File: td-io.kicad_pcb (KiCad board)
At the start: 2 copper layers, 66.5 x 54 mm, 15 parts, among them J1 Conn_02x10_Odd_Even, J2 USB_B, J3 Conn_01x03, J4 Conn_01x02, Q1 AO4818B, U1 Pico, U2 ISL3175EIBZ-T

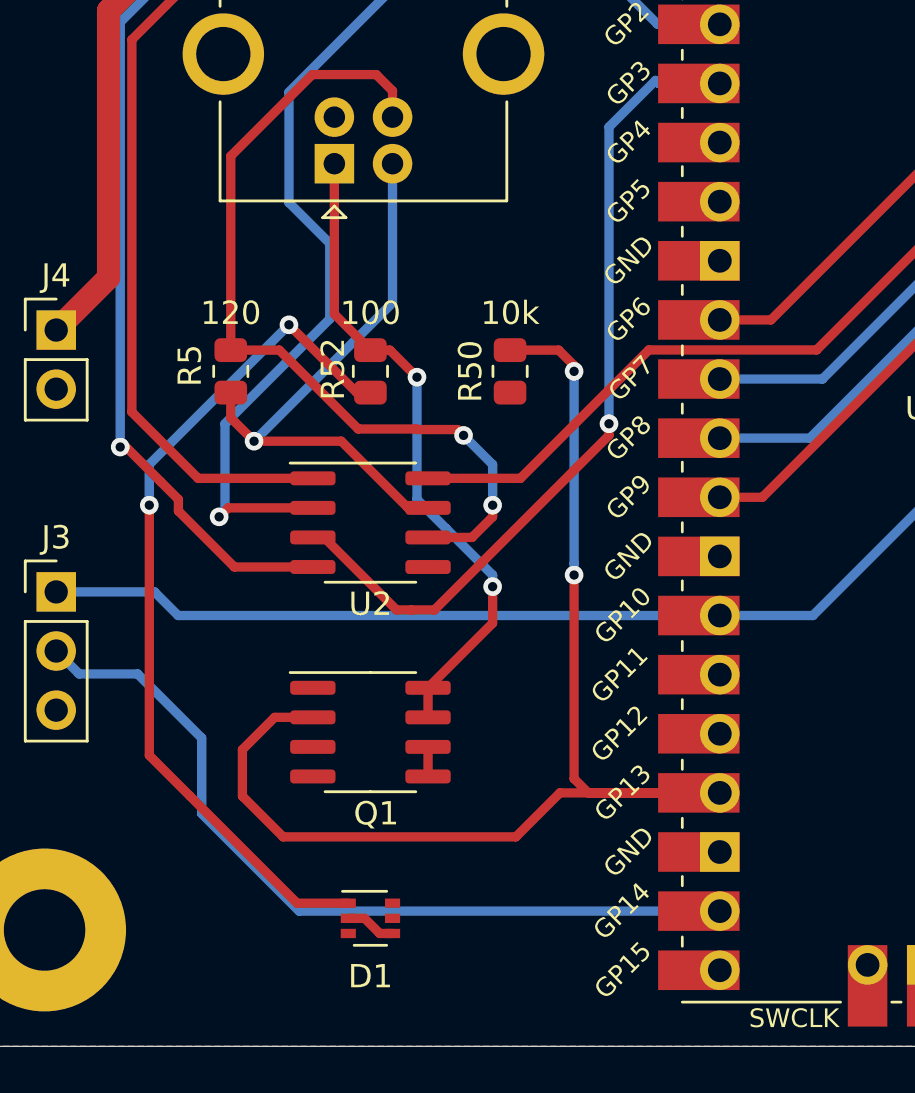
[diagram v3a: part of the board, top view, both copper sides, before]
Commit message: Add some breakout pins
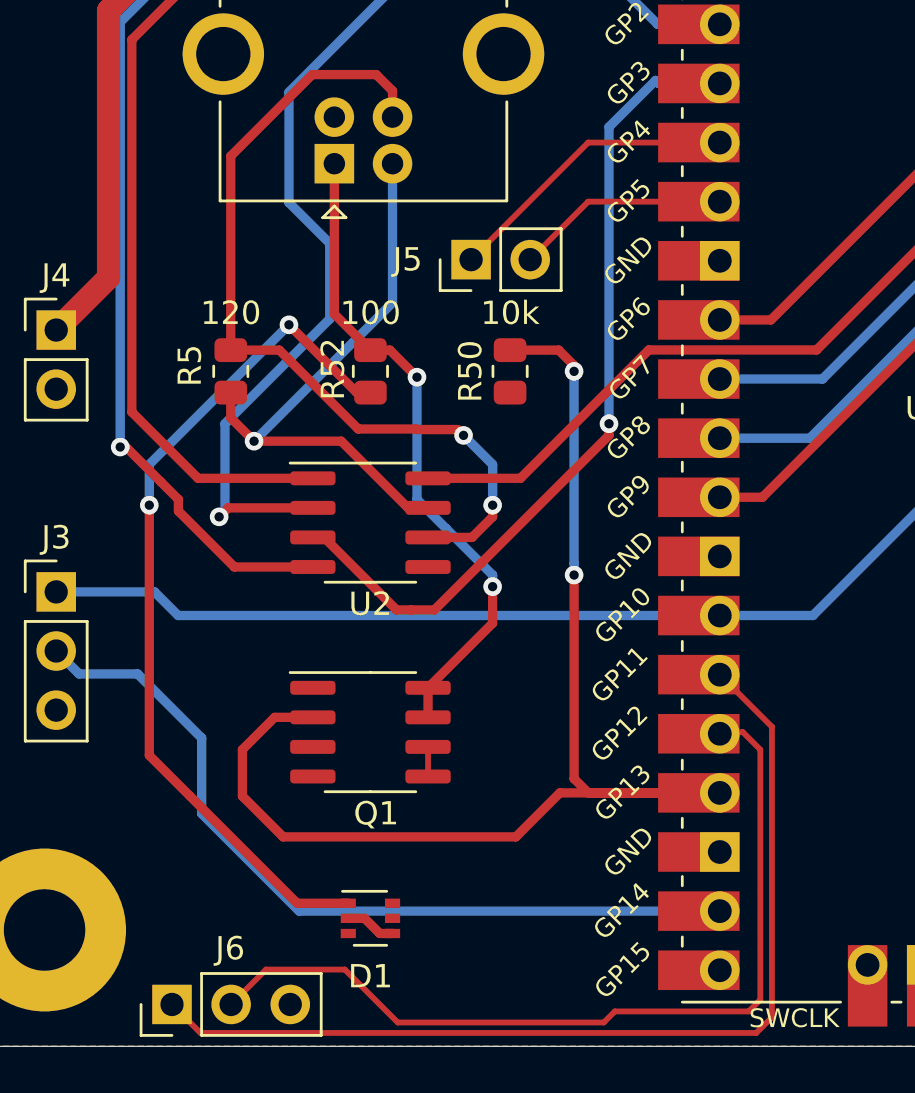
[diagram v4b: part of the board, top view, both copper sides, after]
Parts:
- added J5: I2C, Connector_PinHeader_2.54mm:PinHeader_1x02_P2.54mm_Vertical, F.Cu at (190.3, 64.2)
- added J6: DIPS, Connector_PinHeader_2.54mm:PinHeader_1x03_P2.54mm_Vertical, F.Cu at (177.5, 96.2)
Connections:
- Q1 pad 5: unconnected-(Q1-Pad5) -> Net-(Q1-Pad5)
- Q1 pad 6: unconnected-(Q1-Pad5) -> Net-(Q1-Pad5)
- U1 pad 6: unconnected-(U1-Pad6) -> Net-(U1-Pad6)
- U1 pad 7: unconnected-(U1-Pad7) -> Net-(U1-Pad7)
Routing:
- net /dip1: track 0.00 -> 42.2 mm
- net /dip2: track 0.00 -> 37.5 mm
- net Net-(U1-Pad6): track 0.00 -> 12.8 mm
- net Net-(U1-Pad7): track 0.00 -> 9.18 mm
- net unconnected-(Q1-Pad5): track 1.27 -> 0.00 mm
- net Net-(Q1-Pad5): track 0.00 -> 1.27 mm

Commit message: Clean up pcb
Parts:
- moved D1 1.46 mm to (186.4, 91.1)
- moved J6 1.03 mm to (178.4, 95.7)
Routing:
- net /dip1: track 42.2 -> 41.5 mm
- net /dip2: track 37.5 -> 37.0 mm
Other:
- board text added: "1"
- board text added: "19"
- board text added: "2"
- board text added: "20"
- board text added: "5V"
- board text added: "GND"
- board text added: "SERVICE"
- board text added: "TEST"
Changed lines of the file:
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@@
   )
   (footprint "Package_TO_SOT_SMD:SOT-363_SC-70-6" (layer "F.Cu")
-    (at 186 92.5)
+    (at 186.4 91.1)
     (descr "SOT-363, SC-70-6")
     (tags "SOT-363 SC-70-6")
@@
     (property "Sheetname" "")
     (attr smd)
-    (fp_text reference "D1" (at 0 2.5) (layer "F.SilkS")
+    (fp_text reference "D1" (at 2.7 0.1) (layer "F.SilkS")
       (effects (font (size 1 1) (thickness 0.15)))
     )
@@
     (property "Sheetname" "")
     (attr smd)
-    (fp_text reference "Q1" (at 0.25 3.5) (layer "F.SilkS")
+    (fp_text reference "Q1" (at 5.4 0.2) (layer "F.SilkS")
       (effects (font (size 1 1) (thickness 0.15)))
     )
@@
     (property "Sheetname" "")
     (attr smd)
-    (fp_text reference "U2" (at 0 3.5) (layer "F.SilkS")
+    (fp_text reference "U2" (at 5.1 0.7) (layer "F.SilkS")
       (effects (font (size 1 1) (thickness 0.15)))
     )
@@
     (property "Sheetname" "")
     (attr through_hole)
-    (fp_text reference "J2" (at 8.2275 1.05 270) (layer "F.SilkS")
+    (fp_text reference "J2" (at 8.2275 1.05) (layer "F.SilkS")
       (effects (font (size 1 1) (thickness 0.15)))
     )
@@
     (property "Sheetname" "")
     (attr through_hole)
-    (fp_text reference "J4" (at 0 -2.33) (layer "F.SilkS")
+    (fp_text reference "J4" (at -0.1 -3.425) (layer "F.SilkS")
       (effects (font (size 1 1) (thickness 0.15)))
     )
@@
     (property "Sheetname" "")
     (attr through_hole)
-    (fp_text reference "J1" (at 1.27 -2.33) (layer "F.SilkS")
+    (fp_text reference "J1" (at -2.56 19.54) (layer "F.SilkS")
       (effects (font (size 1 1) (thickness 0.15)))
     )
@@
   )
   (footprint "Connector_PinHeader_2.54mm:PinHeader_1x03_P2.54mm_Vertical" (layer "F.Cu")
-    (at 177.475 96.2 90)
+    (at 178.375 95.7 90)
     (descr "Through hole straight pin header, 1x03, 2.54mm pitch, single row")
     (tags "Through hole pin header THT 1x03 2.54mm single row")
@@
     (property "Sheetname" "")
     (attr through_hole)
-    (fp_text reference "J6" (at 2.4 2.5 180) (layer "F.SilkS")
+    (fp_text reference "J6" (at 0 8.325 180) (layer "F.SilkS")
       (effects (font (size 1 1) (thickness 0.15)))
     )
@@
     (property "Sheetname" "")
     (attr through_hole)
-    (fp_text reference "J3" (at 0 -2.33) (layer "F.SilkS")
+    (fp_text reference "J3" (at 0 -3.275) (layer "F.SilkS")
       (effects (font (size 1 1) (thickness 0.15)))
     )
@@
   (gr_line (start 167.5 44) (end 234 44) (layer "Edge.Cuts") (width 0.05))
   (gr_line (start 167.5 98) (end 167.5 44) (layer "Edge.Cuts") (width 0.05))
+  (gr_text "1" (at 228 57.4) (layer "F.SilkS")
+    (effects (font (size 0.8 0.8) (thickness 0.15)))
+  )
+  (gr_text "GND" (at 175.3 83.5) (layer "F.SilkS")
+    (effects (font (size 0.8 0.8) (thickness 0.15)) (justify left))
+  )
+  (gr_text "20" (at 230.5 85.3) (layer "F.SilkS")
+    (effects (font (size 0.8 0.8) (thickness 0.15)))
+  )
+  (gr_text "2" (at 230.5 57.4) (layer "F.SilkS")
+    (effects (font (size 0.8 0.8) (thickness 0.15)))
+  )
+  (gr_text "5V" (at 175.8 67.2) (layer "F.SilkS")
+    (effects (font (size 0.8 0.8) (thickness 0.15)))
+  )
+  (gr_text "SERVICE" (at 175.3 81) (layer "F.SilkS")
+    (effects (font (size 0.8 0.8) (thickness 0.15)) (justify left))
+  )
+  (gr_text "TEST" (at 176.7 78.5) (layer "F.SilkS")
+    (effects (font (size 0.8 0.8) (thickness 0.15)))
+  )
+  (gr_text "19" (at 228 85.3) (layer "F.SilkS")
+    (effects (font (size 0.8 0.8) (thickness 0.15)))
+  )
+  (gr_text "GND" (at 176 69.7) (layer "F.SilkS")
+    (effects (font (size 0.8 0.8) (thickness 0.15)))
+  )
   (segment (start 184.75 72) (end 181 72) (width 0.4) (layer "F.Cu") (net 2))
   (segment (start 187.615 74.865) (end 184.75 72) (width 0.4) (layer "F.Cu") (net 2))
@@
   (segment (start 178.595 73.595) (end 175.75 70.75) (width 0.4) (layer "F.Cu") (net 12))
   (segment (start 175.75 54.75) (end 181.49 49.01) (width 0.4) (layer "F.Cu") (net 12))
-  (segment (start 186.4 93.15) (end 185.75 92.5) (width 0.4) (layer "F.Cu") (net 13))
-  (segment (start 186.95 93.15) (end 186.4 93.15) (width 0.4) (layer "F.Cu") (net 13))
-  (segment (start 185.75 92.5) (end 185.05 92.5) (width 0.4) (layer "F.Cu") (net 13))
-  (segment (start 178.25 87.25) (end 176.5 85.5) (width 0.4) (layer "F.Cu") (net 14))
+  (segment (start 186.774022 91.75) (end 186.124022 91.1) (width 0.4) (layer "F.Cu") (net 13))
+  (segment (start 187.35 91.75) (end 186.774022 91.75) (width 0.4) (layer "F.Cu") (net 13))
+  (segment (start 186.124022 91.1) (end 185.45 91.1) (width 0.4) (layer "F.Cu") (net 13))
+  (segment (start 185.45 90.45) (end 181.45 90.45) (width 0.4) (layer "F.Cu") (net 14))
   (segment (start 182.5 67) (end 185.4125 69.9125) (width 0.4) (layer "F.Cu") (net 14))
-  (segment (start 185.05 91.85) (end 182.85 91.85) (width 0.4) (layer "F.Cu") (net 14))
   (segment (start 176.5 85.5) (end 176.5 74.75) (width 0.4) (layer "F.Cu") (net 14))
-  (segment (start 182.85 91.85) (end 178.25 87.25) (width 0.4) (layer "F.Cu") (net 14))
   (segment (start 185.4125 69.9125) (end 186 69.9125) (width 0.4) (layer "F.Cu") (net 14))
+  (segment (start 181.45 90.45) (end 176.5 85.5) (width 0.4) (layer "F.Cu") (net 14))
   (via (at 182.5 67) (size 0.8) (drill 0.4) (layers "F.Cu" "B.Cu") (net 14))
   (via (at 176.5 74.75) (size 0.8) (drill 0.4) (layers "F.Cu" "B.Cu") (net 14))
@@
   (segment (start 178.75 88) (end 182.94 92.19) (width 0.4) (layer "B.Cu") (net 44))
   (segment (start 178.75 84.75) (end 178.75 88) (width 0.4) (layer "B.Cu") (net 44))
-  (segment (start 213.420489 44.920489) (end 183.329511 44.920489) (width 1) (layer "F.Cu") (net 45))
-  (segment (start 174.75 53.5) (end 174.75 64.975) (width 1) (layer "F.Cu") (net 45))
-  (segment (start 174.75 64.975) (end 172.5 67.225) (width 1) (layer "F.Cu") (net 45))
+  (segment (start 182.879511 44.920489) (end 172.7 55.1) (width 1) (layer "F.Cu") (net 45))
+  (segment (start 218.79 49.01) (end 217.51 49.01) (width 1) (layer "F.Cu") (net 45))
+  (segment (start 172.7 55.1) (end 172.7 67.025) (width 1) (layer "F.Cu") (net 45))
+  (segment (start 172.7 67.025) (end 172.5 67.225) (width 1) (layer "F.Cu") (net 45))
+  (segment (start 213.420489 44.920489) (end 182.879511 44.920489) (width 1) (layer "F.Cu") (net 45))
   (segment (start 217.51 49.01) (end 213.420489 44.920489) (width 1) (layer "F.Cu") (net 45))
-  (segment (start 218.79 49.01) (end 217.51 49.01) (width 1) (layer "F.Cu") (net 45))
-  (segment (start 183.329511 44.920489) (end 174.75 53.5) (width 1) (layer "F.Cu") (net 45))
-  (segment (start 202.575969 97.424031) (end 178.699031 97.424031) (width 0.25) (layer "F.Cu") (net 46))
   (segment (start 201.01 82.03) (end 203.25 84.27) (width 0.25) (layer "F.Cu") (net 46))
-  (segment (start 178.699031 97.424031) (end 177.475 96.2) (width 0.25) (layer "F.Cu") (net 46))
+  (segment (start 202.575969 97.424031) (end 180.099031 97.424031) (width 0.25) (layer "F.Cu") (net 46))
+  (segment (start 203.25 84.27) (end 203.25 96.75) (width 0.25) (layer "F.Cu") (net 46))
+  (segment (start 180.099031 97.424031) (end 178.375 95.7) (width 0.25) (layer "F.Cu") (net 46))
   (segment (start 203.25 96.75) (end 202.575969 97.424031) (width 0.25) (layer "F.Cu") (net 46))
-  (segment (start 203.25 84.27) (end 203.25 96.75) (width 0.25) (layer "F.Cu") (net 46))
-  (segment (start 196.5 96.5) (end 202.25 96.5) (width 0.25) (layer "F.Cu") (net 47))
-  (segment (start 184.9 94.7) (end 181.515 94.7) (width 0.25) (layer "F.Cu") (net 47))
-  (segment (start 196.025489 96.974511) (end 196.5 96.5) (width 0.25) (layer "F.Cu") (net 47))
-  (segment (start 202.25 96.5) (end 202.75 96) (width 0.25) (layer "F.Cu") (net 47))
-  (segment (start 201.08 84.5) (end 201.01 84.57) (width 0.25) (layer "F.Cu") (net 47))
-  (segment (start 181.515 94.7) (end 180.015 96.2) (width 0.25) (layer "F.Cu") (net 47))
-  (segment (start 202 84.5) (end 201.08 84.5) (width 0.25) (layer "F.Cu") (net 47))
-  (segment (start 184.9 94.7) (end 187.174511 96.974511) (width 0.25) (layer "F.Cu") (net 47))
-  (segment (start 187.174511 96.974511) (end 196.025489 96.974511) (width 0.25) (layer "F.Cu") (net 47))
-  (segment (start 202.75 96) (end 202.75 85.25) (width 0.25) (layer "F.Cu") (net 47))
-  (segment (start 202.75 85.25) (end 202 84.5) (width 0.25) (layer "F.Cu") (net 47))
+  (segment (start 187.174511 96.974511) (end 184.725489 94.525489) (width 0.25) (layer "F.Cu") (net 47))
+  (segment (start 202.25 96.5) (end 196.5 96.5) (width 0.25) (layer "F.Cu") (net 47))
+  (segment (start 202.75 85.25) (end 202.75 96) (width 0.25) (layer "F.Cu") (net 47))
+  (segment (start 196.5 96.5) (end 196.025489 96.974511) (width 0.25) (layer "F.Cu") (net 47))
+  (segment (start 180.915 95.7) (end 180.515 95.7) (width 0.25) (layer "F.Cu") (net 47))
+  (segment (start 196.025489 96.974511) (end 187.174511 96.974511) (width 0.25) (layer "F.Cu") (net 47))
+  (segment (start 182.089511 94.525489) (end 180.915 95.7) (width 0.25) (layer "F.Cu") (net 47))
+  (segment (start 202 84.5) (end 202.75 85.25) (width 0.25) (layer "F.Cu") (net 47))
+  (segment (start 201.08 84.5) (end 202 84.5) (width 0.25) (layer "F.Cu") (net 47))
+  (segment (start 184.725489 94.525489) (end 182.089511 94.525489) (width 0.25) (layer "F.Cu") (net 47))
+  (segment (start 201.01 84.57) (end 201.08 84.5) (width 0.25) (layer "F.Cu") (net 47))
+  (segment (start 202.75 96) (end 202.25 96.5) (width 0.25) (layer "F.Cu") (net 47))
   (zone (net 1) (net_name "GND") (layers F&B.Cu) (hatch edge 0.508)
     (connect_pads (clearance 0.1))
